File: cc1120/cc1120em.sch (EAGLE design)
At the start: 1 part, among them U1 CC1120_RHM_32

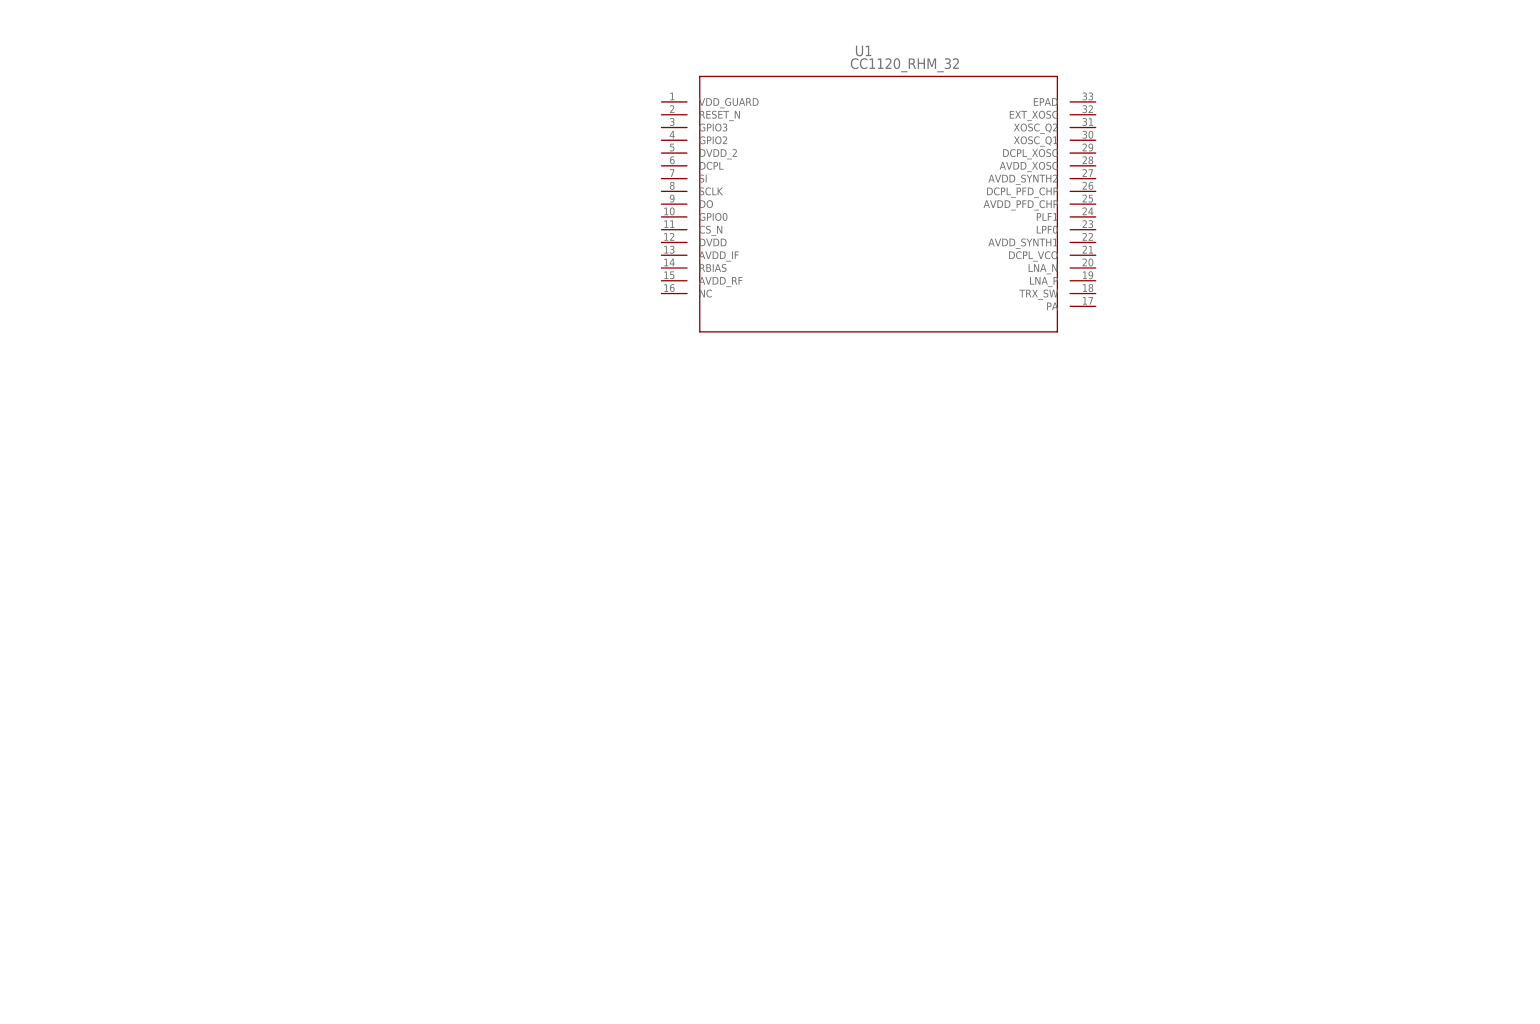
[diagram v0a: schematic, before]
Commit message: CC1120 schematic work.
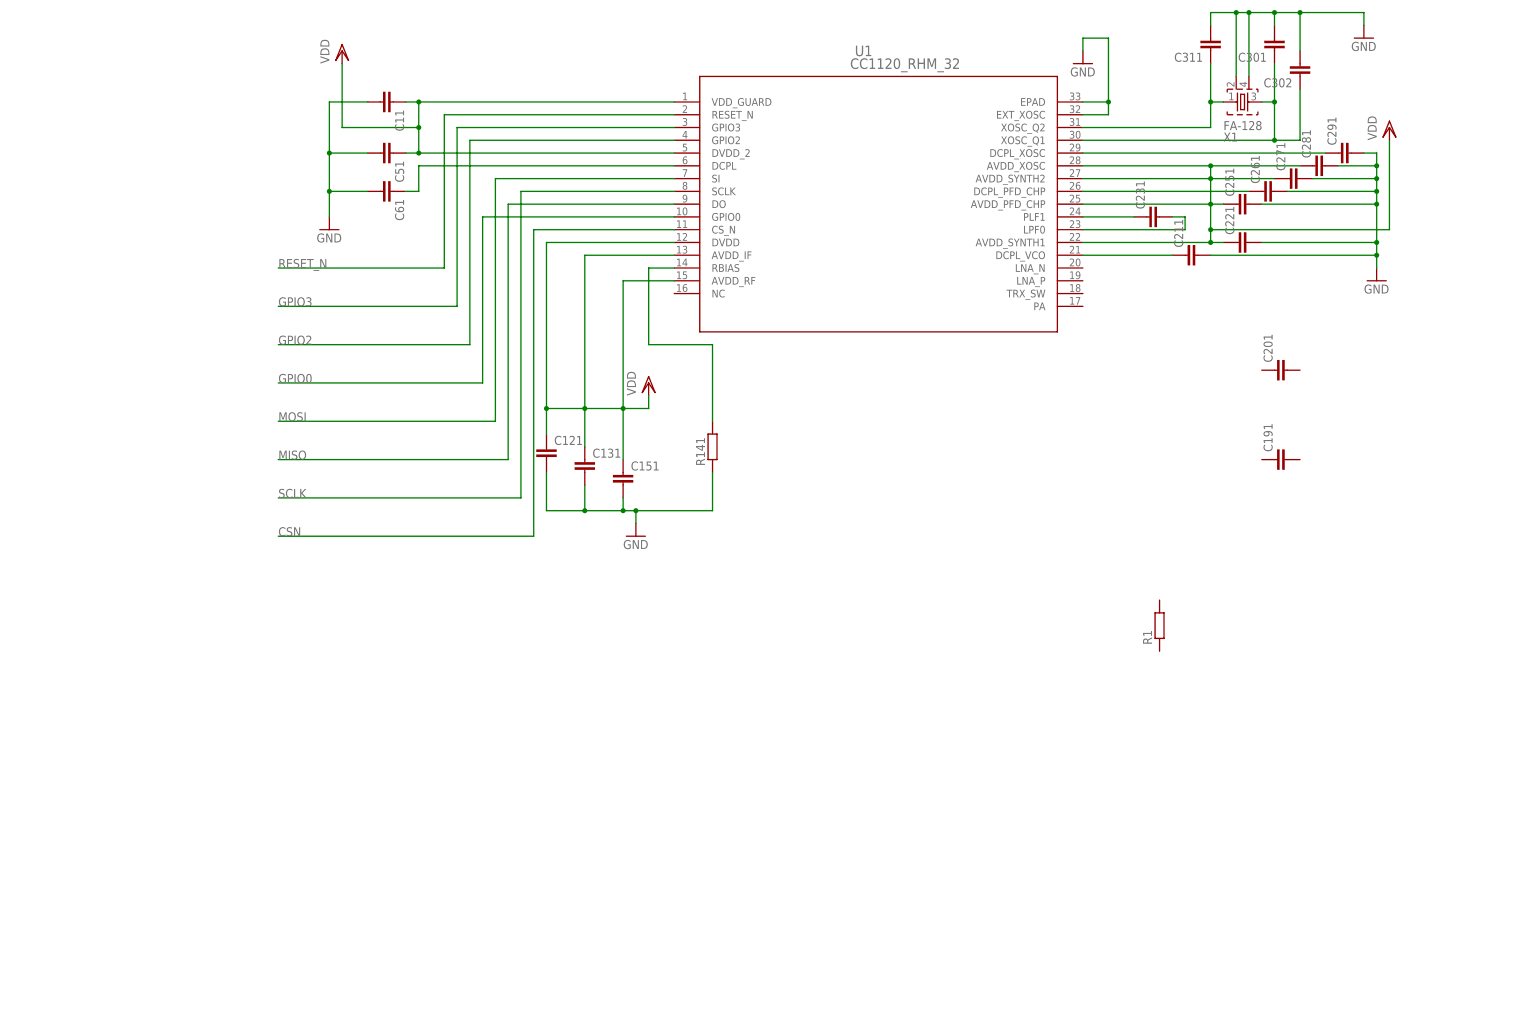
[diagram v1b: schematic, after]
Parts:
- added C11, C121, C131, C151, C191, C201, C211, C221, C231, C251, C261, C271, C281, C291, C301, C302, C311, C51, C61: (no value), rcl:C-EUC0402
- added R1, R141: (no value), rcl:R-EU_R0402
- added X1: FA-128, crystal:FA-128
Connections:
- new net CSN: U1.CS_N
- new net GND: C11.2, C121.2, C131.2, C151.2, C211.2, C221.2, C251.2, C261.2, C271.2, C281.2, C291.2, C301.2, C302.2, C311.2, C51.2, C61.2, R141.1, U1.EPAD, U1.EXT_XOSC, X1.2, X1.4
- new net GPIO0: U1.GPIO0
- new net GPIO2: U1.GPIO2
- new net GPIO3: U1.GPIO3
- new net MISO: U1.DO
- new net MOSI: U1.SI
- new net N$1: C231.1, U1.PLF1
- new net N$13: R141.2, U1.RBIAS
- new net N$2: C231.2, U1.LPF0
- new net N$3: C211.1, U1.DCPL_VCO
- new net N$4: C61.1, U1.DCPL
- new net N$5: C261.1, U1.DCPL_PFD_CHP
- new net N$6: C311.1, U1.XOSC_Q2, X1.1
- new net N$7: C301.1, C302.1, U1.XOSC_Q1, X1.3
- new net N$8: C291.1, U1.DCPL_XOSC
- new net RESET_N: U1.RESET_N
- new net SCLK: U1.SCLK
- new net VDD: C11.1, C121.1, C131.1, C151.1, C221.1, C251.1, C271.1, C281.1, C51.1, U1.AVDD_IF, U1.AVDD_PFD_CHP, U1.AVDD_RF, U1.AVDD_SYNTH1, U1.AVDD_SYNTH2, U1.AVDD_XOSC, U1.DVDD, U1.DVDD_2, U1.VDD_GUARD

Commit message: Work on MS2
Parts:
- removed R1: (no value), rcl:R-EU_R0402
- added C171, C172, C173, C174, C175, C176, C177, C181: C_EU, CC11x:C_EU
- added L171, L172, L173, L174, L191, L192, L193, L201: L_US, CC11x:L_US
- added R12, R171: R_EU, CC11x:R_EU
- C11, C121, C131, C151, C191, C201, C211, C221, C231, C251, C261, C271, C281, C291, C301, C302, C311, C51, C61: value (none) -> C_EU; device rcl:C-EUC0402 -> CC11x:C_EU
- R141: value (none) -> R_EU; device rcl:R-EU_R0402 -> CC11x:R_EU
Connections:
- new net N$10: C191.1, L191.2, L192.1, U1.LNA_P
- new net N$11: C191.2, L193.1, L201.2
- new net N$12: C181.1, L193.2, U1.TRX_SW
- new net N$14: C174.1, L171.2, U1.PA
- new net N$15: C174.2, C176.1, L172.1
- new net N$16: C176.2, C181.2, L172.2, L173.1
- new net N$17: C175.1, C177.1, L173.2, L174.1
- new net N$18: C177.2, L174.2
- new net N$19: C173.1, L171.1, R171.2
- new net N$9: C201.1, L191.1, L201.1, U1.LNA_N
- net GND: now also C171.2, C172.2, C175.2, C201.2, L192.2, R12.1, R12.2
- net VDD: now also C171.1, C172.1, C173.2, R171.1
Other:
- moved on the sheet: C11, C191, C201, C51, C61

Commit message: Work on CC2538 Z1 board
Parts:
- added ANT_868: SMA, CC11x:SMA
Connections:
- net GND: now also ANT_868.1, ANT_868.2
- net N$18: now also ANT_868.RF
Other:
- moved on the sheet: C11, C121, C131, C151, C171, C172, C173, C174, C175, C176, C177, C181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
